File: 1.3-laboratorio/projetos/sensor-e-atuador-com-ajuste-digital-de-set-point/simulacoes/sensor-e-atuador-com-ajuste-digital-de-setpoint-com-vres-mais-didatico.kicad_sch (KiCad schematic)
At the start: 32 parts, among them U1 OPAMP, U2 OPAMP, U3 OPAMP

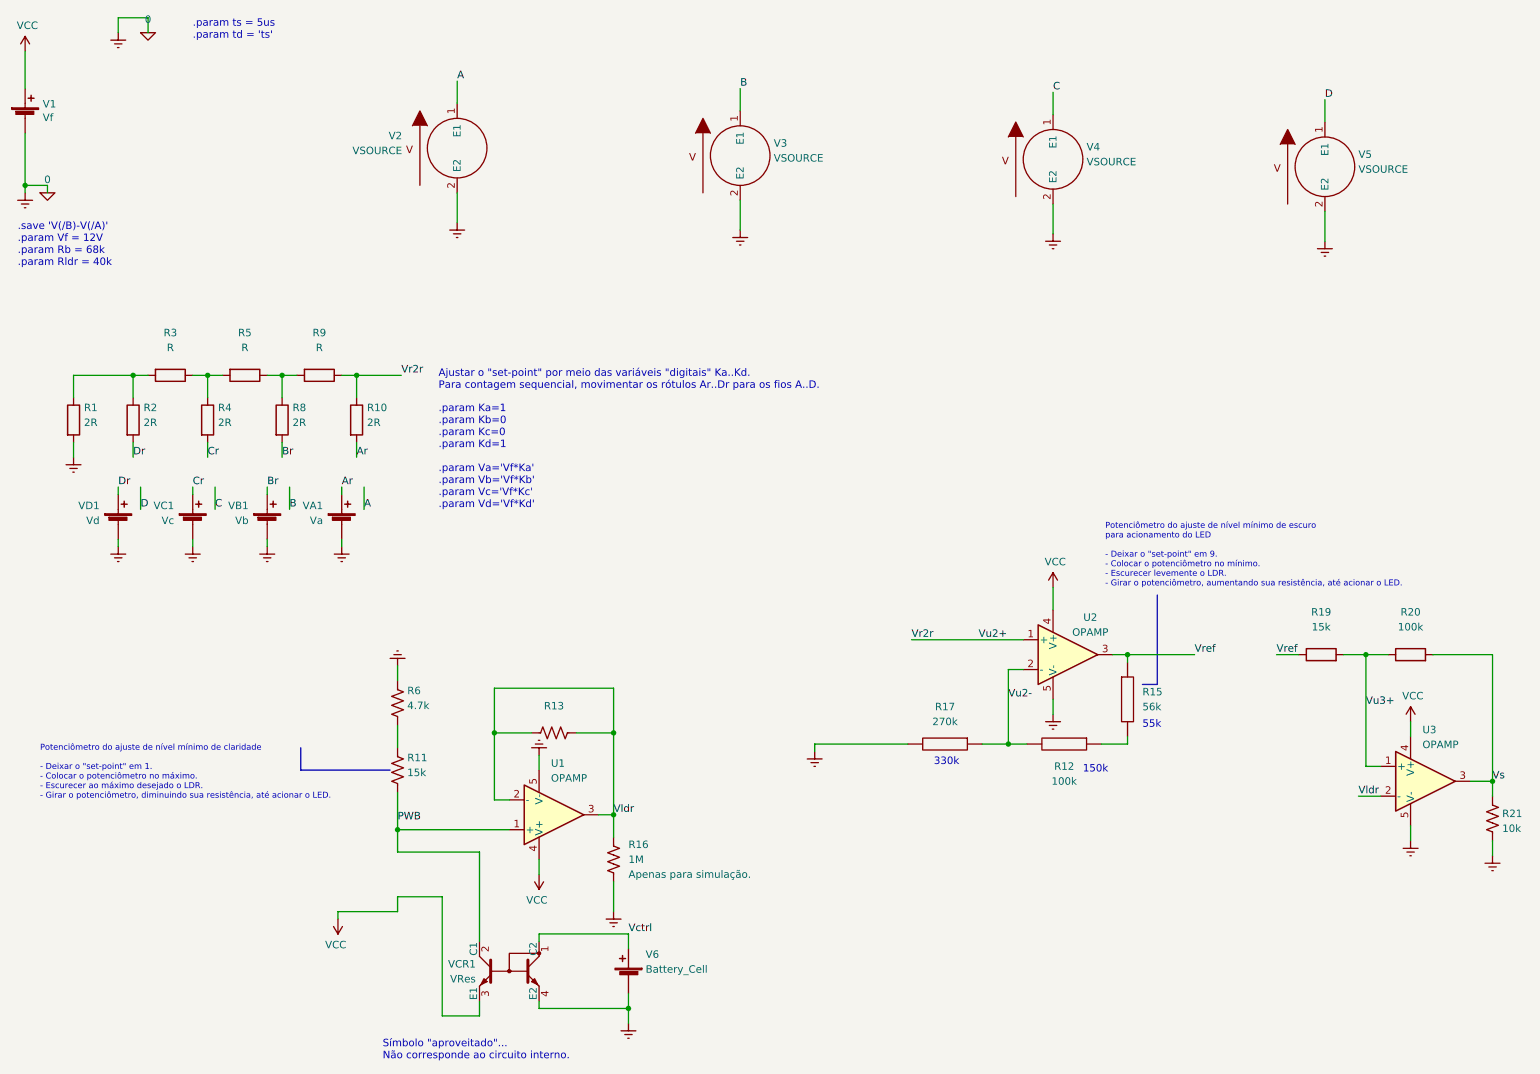
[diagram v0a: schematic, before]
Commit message: Edição da versão didática v. 1.0.0, incluindo informações para depuração, concluída.
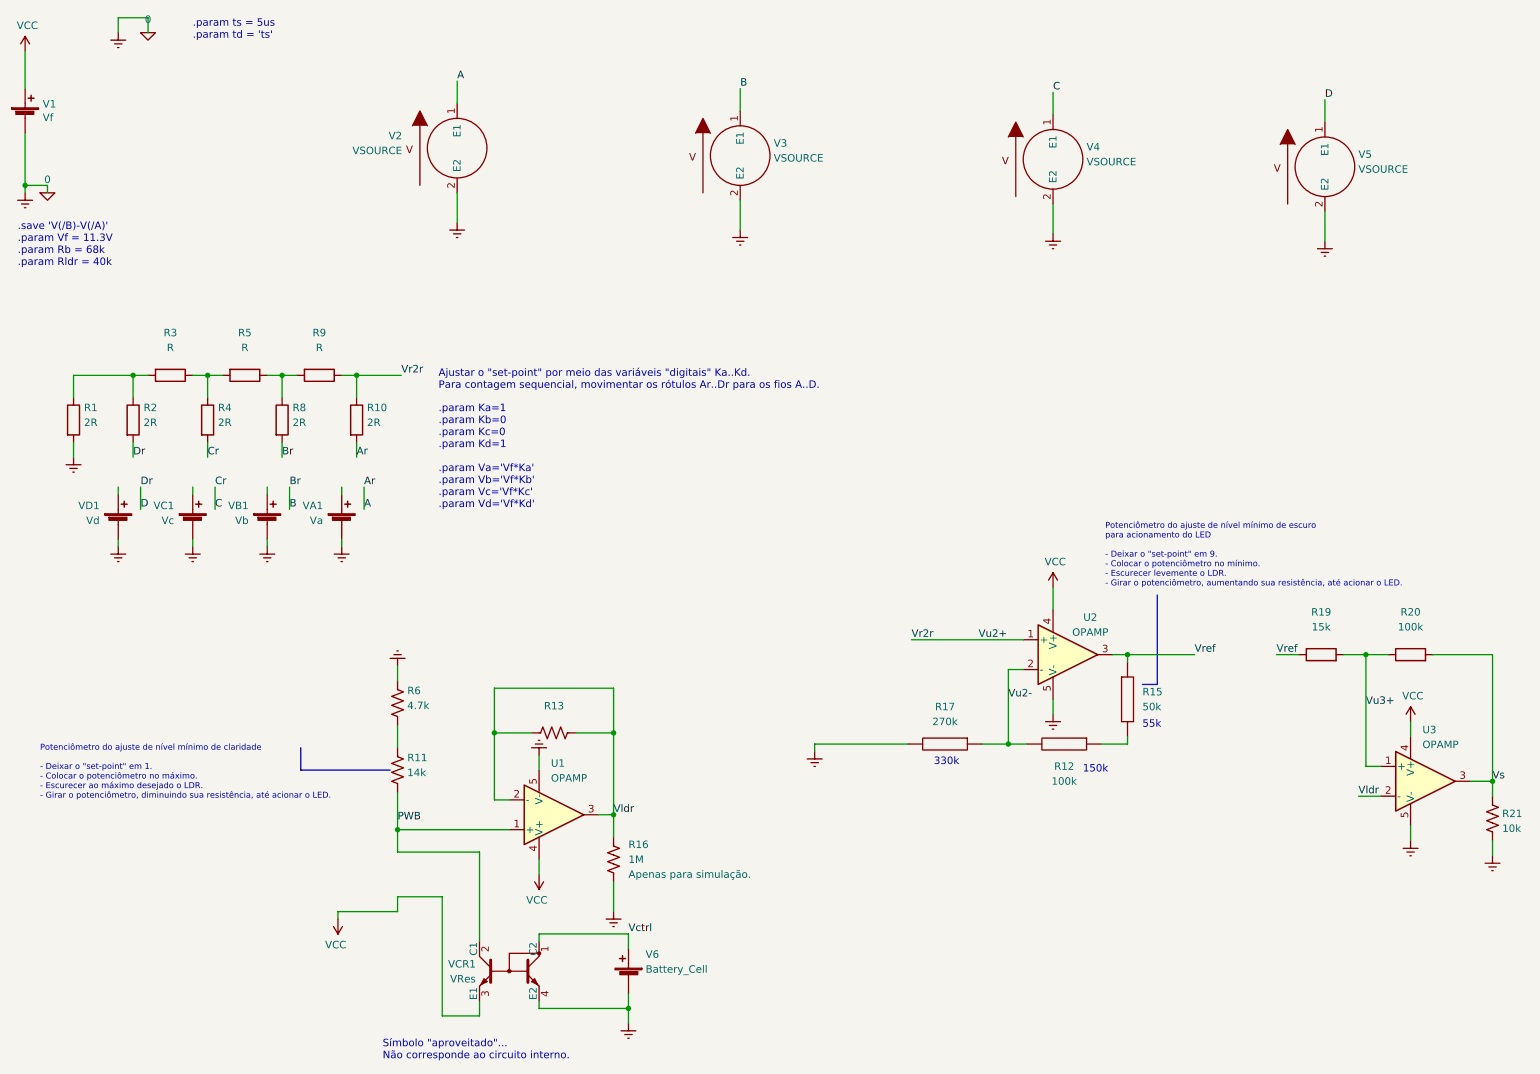
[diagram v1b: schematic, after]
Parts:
- R11: value 15k -> 14k
- R15: value 56k -> 50k
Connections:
- net A: now also R10.2
- net B: now also R8.2
- net C: now also R4.2
- net D: now also R2.2
- net Ar: no longer names the net of VA1.1 (+)
- net Ar: no longer R10.2
- net Br: no longer names the net of VB1.1 (+)
- net Br: no longer R8.2
- net Cr: no longer names the net of VC1.1 (+)
- net Cr: no longer R4.2
- net Dr: no longer names the net of VD1.1 (+)
- net Dr: no longer R2.2
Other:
- note added: ".save 'V(/B)-V(/A)' .param Vf = 11.3V .param Rb = 68k .param Rldr = 40k"
- note removed: ".save 'V(/B)-V(/A)' .param Vf = 12V .param Rb = 68k .param Rldr = 40k"
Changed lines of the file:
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@@
     (effects (font (size 1.27 1.27)) (justify left bottom))
   )
-  (text ".save 'V(/B)-V(/A)'\n.param Vf = 12V\n.param Rb = 68k\n.param Rldr = 40k"
+  (text ".save 'V(/B)-V(/A)'\n.param Vf = 11.3V\n.param Rb = 68k\n.param Rldr = 40k"
     (at 16.51 59.055 0)
     (effects (font (size 1.27 1.27)) (justify left bottom))
@@
     (effects (font (size 1.27 1.27)) (justify left bottom))
   )
-  (label "Ar" (at 71.755 96.52 0) (fields_autoplaced)
+  (label "Ar" (at 75.565 96.52 0) (fields_autoplaced)
     (effects (font (size 1.27 1.27)) (justify left bottom))
   )
@@
     (effects (font (size 1.27 1.27)) (justify left bottom))
   )
-  (label "Br" (at 59.055 96.52 0) (fields_autoplaced)
+  (label "Br" (at 62.865 96.52 0) (fields_autoplaced)
     (effects (font (size 1.27 1.27)) (justify left bottom))
   )
@@
     (effects (font (size 1.27 1.27)) (justify left bottom))
   )
-  (label "Dr" (at 33.655 96.52 0) (fields_autoplaced)
+  (label "Dr" (at 37.465 96.52 0) (fields_autoplaced)
     (effects (font (size 1.27 1.27)) (justify left bottom))
   )
@@
     (effects (font (size 1.27 1.27)) (justify left bottom))
   )
-  (label "Cr" (at 46.355 96.52 0) (fields_autoplaced)
+  (label "Cr" (at 50.165 96.52 0) (fields_autoplaced)
     (effects (font (size 1.27 1.27)) (justify left bottom))
   )
@@
       (effects (font (size 1.27 1.27)) (justify left))
     )
-    (property "Value" "15k" (at 82.931 145.2138 0)
+    (property "Value" "14k" (at 82.931 145.2138 0)
       (effects (font (size 1.27 1.27)) (justify left))
     )
@@
       (effects (font (size 1.27 1.27)) (justify left))
     )
-    (property "Value" "56k" (at 208.28 133.985 0)
-      (effects (font (size 1.27 1.27)) (justify left))
-    )
+    (property "Value" "50k" (at 208.28 133.985 0)
+      (effects (font (size 1.27 1.27)) (justify left))
+    )

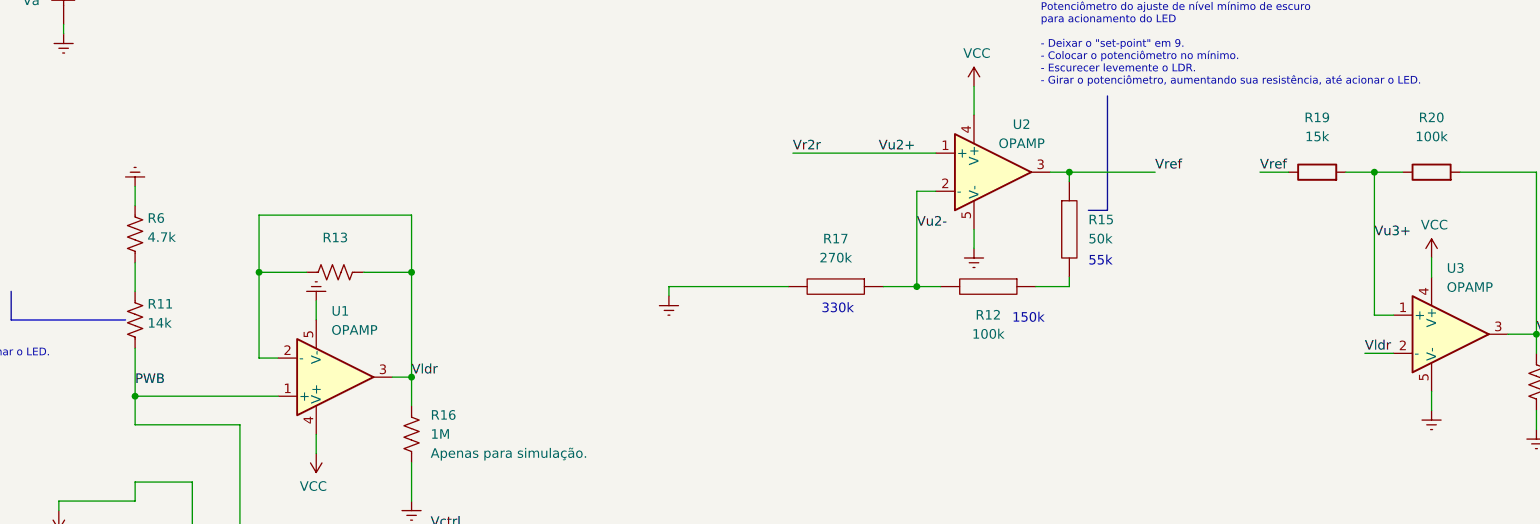
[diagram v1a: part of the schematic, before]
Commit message: Ajustes feitos no esquema elétrico.
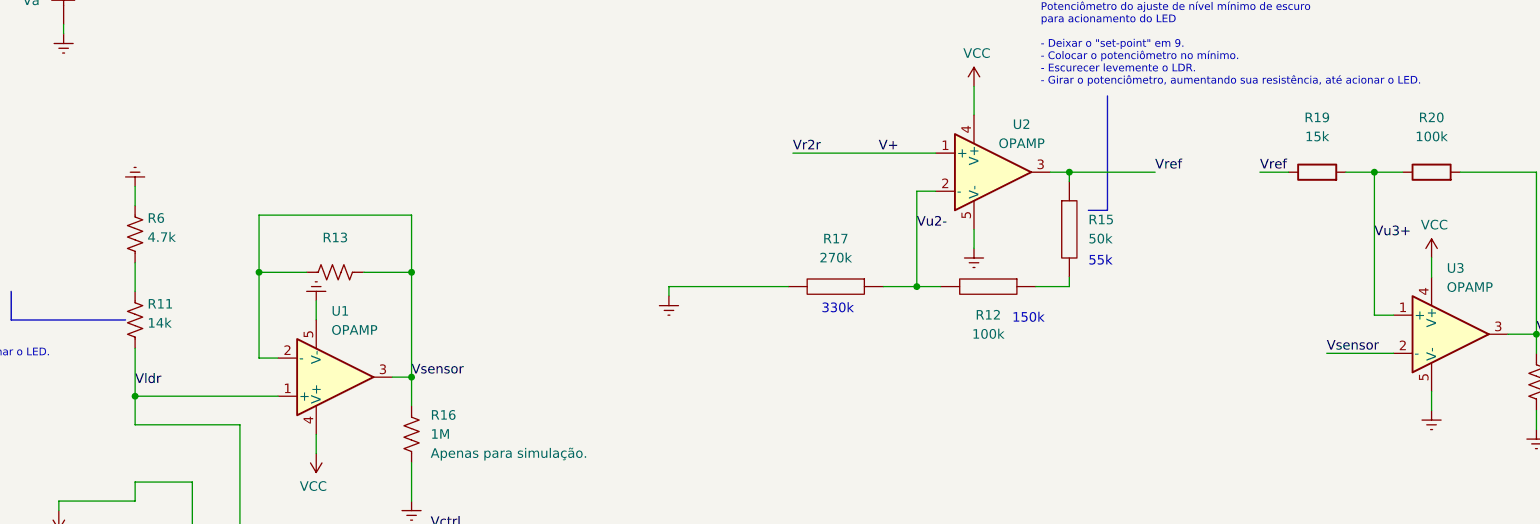
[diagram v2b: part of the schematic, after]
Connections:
- net PWB is gone; now on net Vldr: R11.2, U1.1 (+), VCR1.2 (C1)
- net Vldr: no longer R13.1, R13.2, R16.2, U1.2 (-), U1.3, U3.2 (-)
- net Vr2r renamed V+
- new net Vsensor: R13.1, R13.2, R16.2, U1.2 (-), U1.3, U3.2 (-)
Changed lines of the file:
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@@
     (stroke (width 0) (type default))
   )
-  (wire (pts (xy 245.11 149.225) (xy 248.92 149.225))
+  (wire (pts (xy 240.03 149.225) (xy 248.92 149.225))
     (stroke (width 0) (type default))
   )
@@
     (effects (font (size 1.27 1.27)) (justify left bottom))
   )
-  (label "Vu2+" (at 180.34 122.555 0) (fields_autoplaced)
-    (effects (font (size 1.27 1.27)) (justify left bottom))
-  )
-  (label "Vldr" (at 245.11 149.225 0) (fields_autoplaced)
-    (effects (font (size 1.27 1.27)) (justify left bottom))
-  )
-  (label "Vldr" (at 118.11 152.4 0) (fields_autoplaced)
+  (label "V+" (at 180.34 122.555 0) (fields_autoplaced)
+    (effects (font (size 1.27 1.27)) (justify left bottom))
+  )
+  (label "Vsensor" (at 240.03 149.225 0) (fields_autoplaced)
+    (effects (font (size 1.27 1.27)) (justify left bottom))
+  )
+  (label "Vldr" (at 81.28 153.67 0) (fields_autoplaced)
     (effects (font (size 1.27 1.27)) (justify left bottom))
   )
@@
     (effects (font (size 1.27 1.27)) (justify left bottom))
   )
-  (label "PWB" (at 81.28 153.67 0) (fields_autoplaced)
-    (effects (font (size 1.27 1.27)) (justify left bottom))
-  )
+  (label "Vsensor" (at 118.11 152.4 0) (fields_autoplaced)
+    (effects (font (size 1.27 1.27)) (justify left bottom))
+  )
